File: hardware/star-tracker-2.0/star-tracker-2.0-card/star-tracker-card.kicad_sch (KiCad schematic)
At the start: 8 parts, among them J1 SM14B-SHLS-TF, J101 3-1734592-64-1734592-0, J4 TFM-120-01-L-D-RA, J7 GRPB041VWVN-RC

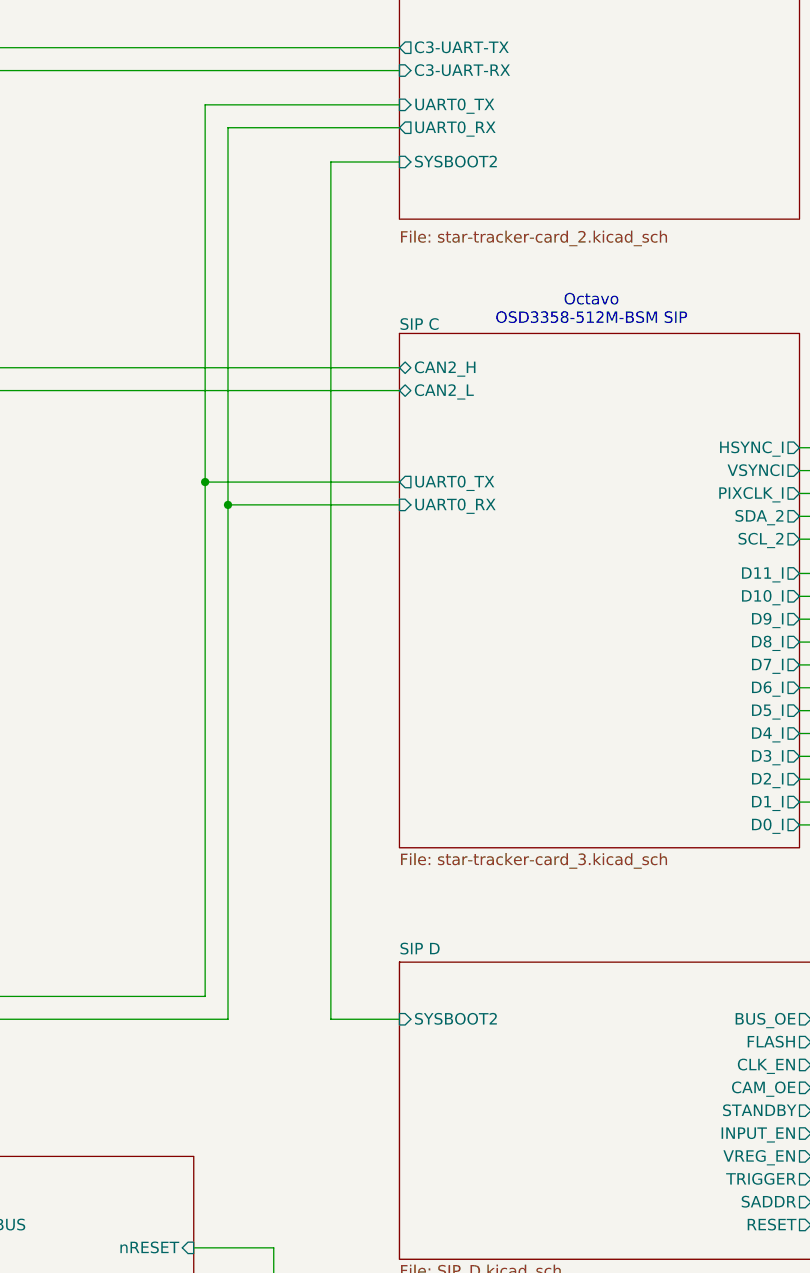
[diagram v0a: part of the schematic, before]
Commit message: Added IMU
added IMU, and i2c pull up resistors to schematic.
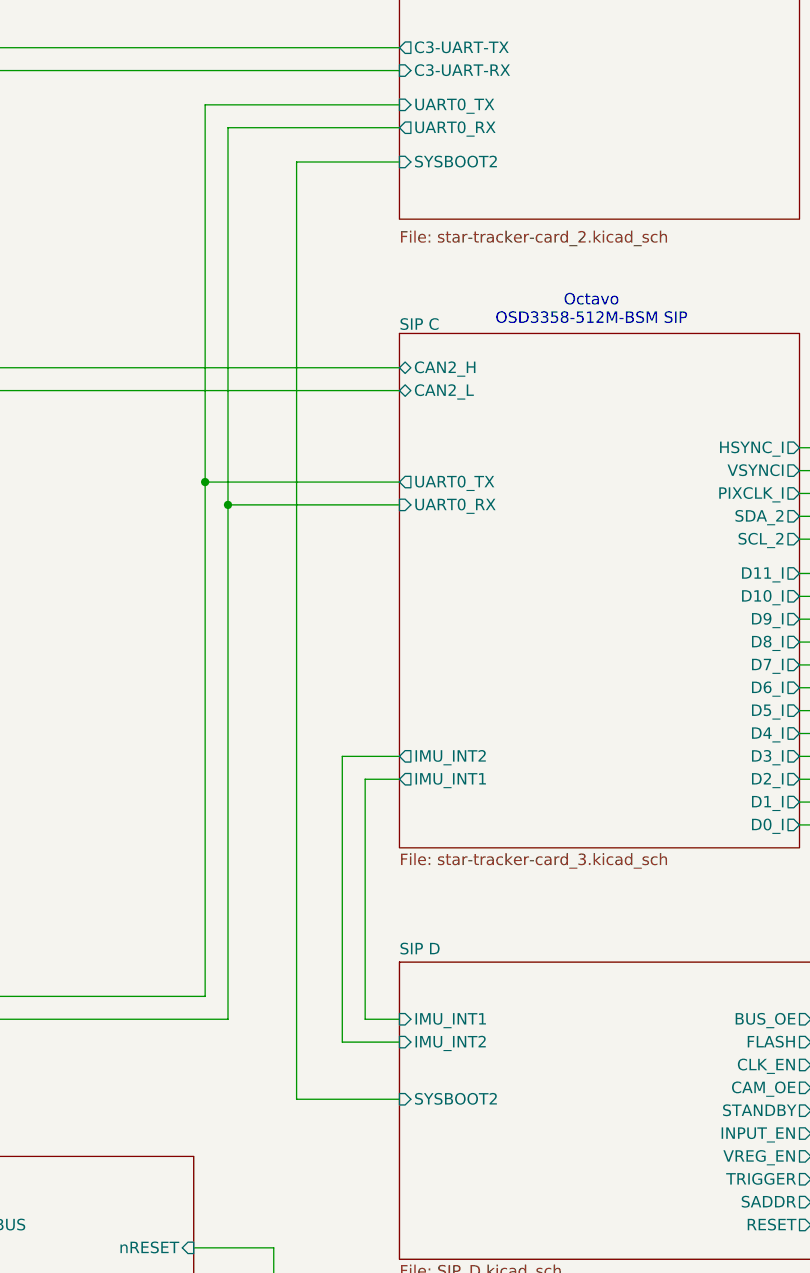
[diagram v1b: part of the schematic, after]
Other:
- sheet SIP C ports: added IMU_INT1, IMU_INT2; removed none
- sheet SIP D ports: added IMU_INT1, IMU_INT2; removed none
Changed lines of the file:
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@@
 	(wire
 		(pts
+			(xy 184.15 179.07) (xy 190.5 179.07)
+		)
+		(stroke
+			(width 0)
+			(type default)
+		)
+	)
+	(wire
+		(pts
 			(xy 386.08 106.68) (xy 386.08 104.14)
 		)
@@
 	(wire
 		(pts
+			(xy 184.15 147.32) (xy 184.15 179.07)
+		)
+		(stroke
+			(width 0)
+			(type default)
+		)
+	)
+	(wire
+		(pts
 			(xy 171.45 119.38) (xy 190.5 119.38)
 		)
@@
 	(wire
 		(pts
+			(xy 190.5 149.86) (xy 186.69 149.86)
+		)
+		(stroke
+			(width 0)
+			(type default)
+		)
+	)
+	(wire
+		(pts
 			(xy 308.61 137.16) (xy 391.16 137.16)
 		)
@@
 	(wire
 		(pts
+			(xy 186.69 149.86) (xy 186.69 176.53)
+		)
+		(stroke
+			(width 0)
+			(type default)
+		)
+	)
+	(wire
+		(pts
 			(xy 46.99 86.36) (xy 49.53 86.36)
 		)
@@
 	(wire
 		(pts
+			(xy 190.5 147.32) (xy 184.15 147.32)
+		)
+		(stroke
+			(width 0)
+			(type default)
+		)
+	)
+	(wire
+		(pts
 			(xy 92.71 199.39) (xy 134.62 199.39)
 		)
@@
 	(wire
 		(pts
+			(xy 186.69 176.53) (xy 190.5 176.53)
+		)
+		(stroke
+			(width 0)
+			(type default)
+		)
+	)
+	(wire
+		(pts
 			(xy 236.22 194.31) (xy 265.43 194.31)
 		)
@@
 	(wire
 		(pts
-			(xy 182.88 81.28) (xy 190.5 81.28)
+			(xy 179.07 81.28) (xy 190.5 81.28)
 		)
 		(stroke
@@
 	(wire
 		(pts
-			(xy 182.88 176.53) (xy 182.88 81.28)
+			(xy 179.07 185.42) (xy 179.07 81.28)
 		)
 		(stroke
@@
 	(wire
 		(pts
-			(xy 190.5 176.53) (xy 182.88 176.53)
+			(xy 190.5 185.42) (xy 179.07 185.42)
 		)
 		(stroke
@@
 		)
 		(pin "SYSBOOT2" input
+			(at 190.5 185.42 180)
+			(effects
+				(font
+					(size 1.27 1.27)
+				)
+				(justify left)
+			)
+		)
+		(pin "IMU_INT1" input
 			(at 190.5 176.53 180)
 			(effects
@@
 			)
 		)
+		(pin "IMU_INT2" input
+			(at 190.5 179.07 180)
+			(effects
+				(font
+					(size 1.27 1.27)
+				)
+				(justify left)
+			)
+		)
 		(instances
 			(project "star-tracker-card"
@@
 			)
 		)
+		(pin "IMU_INT1" output
+			(at 190.5 149.86 180)
+			(effects
+				(font
+					(size 1.27 1.27)
+				)
+				(justify left)
+			)
+		)
+		(pin "IMU_INT2" output
+			(at 190.5 147.32 180)
+			(effects
+				(font
+					(size 1.27 1.27)
+				)
+				(justify left)
+			)
+		)

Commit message: Routine Push
Updated schematic and layout. about 60% done with routing.
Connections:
- net 3.3V: now also J101.4, J101.5, J101.6; no longer J101.31, J101.32, J101.33
- net CLK_EN_E: now also J101.26; no longer J101.23
- net D0_E: now also J101.25; no longer J101.12
- net D10_E: now also J101.12; no longer J101.16
- net D11_E: now also J101.11; no longer J101.17
- net D1_E: now also J101.24; no longer J101.11
- net D2_E: now also J101.23; no longer J101.10
- net D3_E: now also J101.22; no longer J101.9
- net D4_E: now also J101.21; no longer J101.8
- net D5_E: now also J101.20; no longer J101.7
- net D6_E: now also J101.16; no longer J101.6
- net D7_E: now also J101.15; no longer J101.13
- net D9_E: now also J101.13; no longer J101.15
- net FLASH_E: now also J101.31; no longer J101.28
- net GND: now also J101.17, J101.3; no longer J101.20, J101.34
- net HSYNC_E: now also J101.34; no longer J101.4
- net I2C2_SCL: now also J101.9; no longer J101.21
- net I2C2_SDA: now also J101.10; no longer J101.22
- net PIXCLK_E: now also J101.27; no longer J101.5
- net SADDR_E: now also J101.8; no longer J101.27
- net STANDBY_E: now also J101.29; no longer J101.25
- net TRIGGER_E: now also J101.32; no longer J101.29
- net VREG_EN_E: now also J101.7; no longer J101.30
- net VSYNC_E: now also J101.33; no longer J101.3
- net ~{OE_E}: now also J101.30; no longer J101.26
- net ~{RESET_E}: now also J101.28; no longer J101.24
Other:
- moved on the sheet: C42, C43

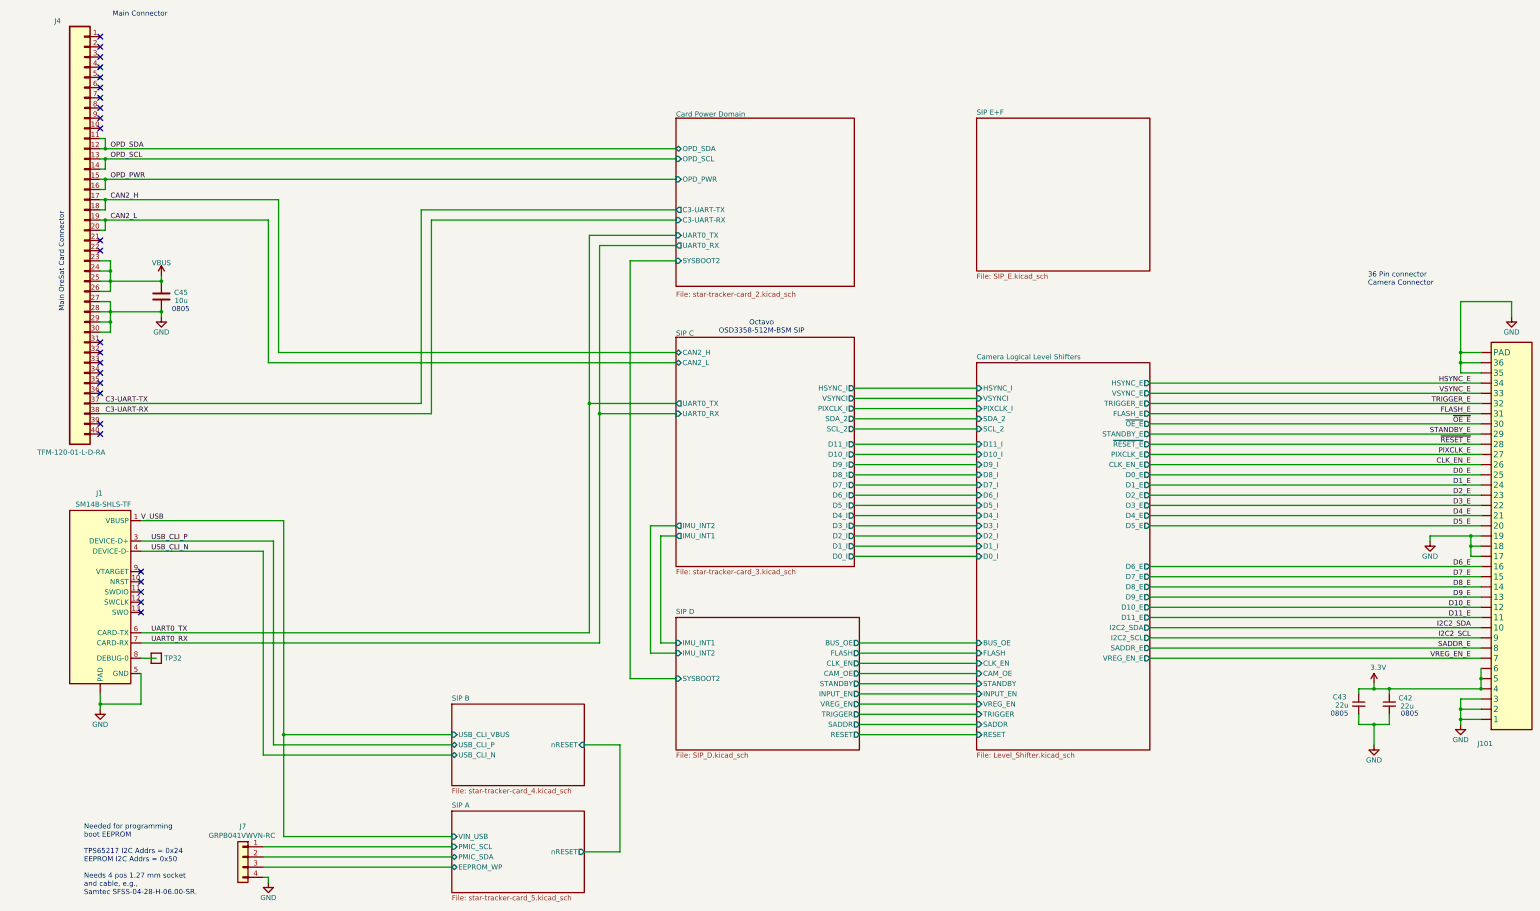
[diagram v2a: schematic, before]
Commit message: Star tracker board update
Added 3d models to footprints, reannotated component designators
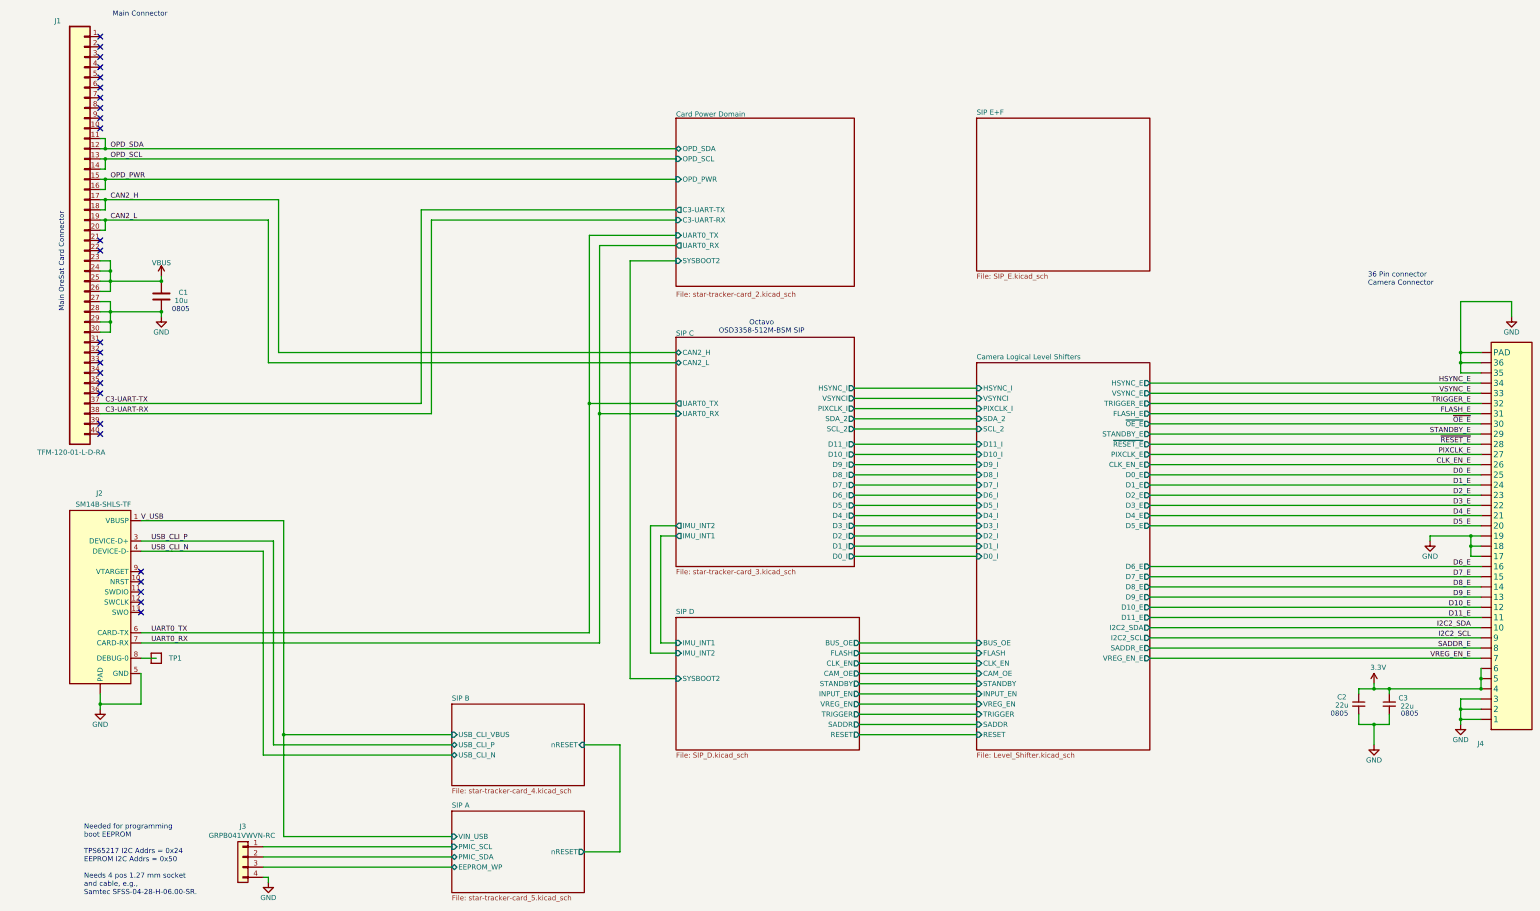
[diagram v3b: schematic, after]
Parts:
- renumbered C45 to C1, C43 to C2, C42 to C3, J4 to J1, J1 to J2, J7 to J3, J101 to J4, TP32 to TP1
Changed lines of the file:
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@@
 	(title_block
 		(title "OreSat Star Tracker")
-		(date "2026-04-22")
-		(rev "1.3")
+		(date "2026-06-05")
+		(rev "2.0")
 		(company "Portland State Aerospace Society")
 	)
@@
 		(in_pos_files yes)
 		(dnp no)
-		(property "Reference" "C42"
+		(property "Reference" "C3"
 			(at 370.586 191.008 0)
 			(show_name no)
@@
 			(project "star-tracker-card"
 				(path "/324e9eb5-7420-4b7e-862c-cc20bb28618a"
-					(reference "C42")
+					(reference "C3")
 					(unit 1)
 				)
@@
 		(in_pos_files yes)
 		(dnp no)
-		(property "Reference" "J1"
+		(property "Reference" "J2"
 			(at 45.974 139.954 0)
 			(show_name no)
@@
 			(project "star-tracker-card"
 				(path "/324e9eb5-7420-4b7e-862c-cc20bb28618a"
-					(reference "J1")
+					(reference "J2")
 					(unit 1)
 				)
@@
 		(in_pos_files yes)
 		(dnp no)
-		(property "Reference" "C45"
+		(property "Reference" "C1"
 			(at 68.834 89.916 0)
 			(show_name no)
@@
 			(project "star-tracker-card"
 				(path "/324e9eb5-7420-4b7e-862c-cc20bb28618a"
-					(reference "C45")
+					(reference "C1")
 					(unit 1)
 				)
@@
 		(in_pos_files yes)
 		(dnp no)
-		(property "Reference" "C43"
+		(property "Reference" "C2"
 			(at 357.632 190.754 0)
 			(show_name no)
@@
 			(project "star-tracker-card"
 				(path "/324e9eb5-7420-4b7e-862c-cc20bb28618a"
-					(reference "C43")
+					(reference "C2")
 					(unit 1)
 				)
@@
 		(in_pos_files yes)
 		(dnp no)
-		(property "Reference" "TP32"
+		(property "Reference" "TP1"
 			(at 67.31 180.34 0)
 			(show_name no)
@@
 			(project "star-tracker-card"
 				(path "/324e9eb5-7420-4b7e-862c-cc20bb28618a"
-					(reference "TP32")
+					(reference "TP1")
 					(unit 1)
 				)
@@
 		(in_pos_files yes)
 		(dnp no)
-		(property "Reference" "#PWR1"
+		(property "Reference" "#PWR02"
 			(at 62.23 101.6 0)
 			(hide yes)
@@
 			(project "star-tracker-card"
 				(path "/324e9eb5-7420-4b7e-862c-cc20bb28618a"
-					(reference "#PWR1")
+					(reference "#PWR02")
 					(unit 1)
 				)
@@
 		(in_pos_files yes)
 		(dnp no)
-		(property "Reference" "#3V-13"
+		(property "Reference" "#3V-01"
 			(at 364.49 184.15 0)
 			(hide yes)
@@
 			(project "star-tracker-card"
 				(path "/324e9eb5-7420-4b7e-862c-cc20bb28618a"
-					(reference "#3V-13")
+					(reference "#3V-01")
 					(unit 1)
 				)
@@
 		(in_pos_files yes)
 		(dnp no)
-		(property "Reference" "#PWR45"
+		(property "Reference" "#PWR06"
 			(at 386.08 203.2 0)
 			(hide yes)
@@
 			(project "star-tracker-card"
 				(path "/324e9eb5-7420-4b7e-862c-cc20bb28618a"
-					(reference "#PWR45")
+					(reference "#PWR06")
 					(unit 1)
 				)
@@
 		(in_pos_files yes)
 		(dnp no)
-		(property "Reference" "#PWR4"
+		(property "Reference" "#PWR04"
 			(at 364.49 208.28 0)
 			(hide yes)
@@
 			(project "star-tracker-card"
 				(path "/324e9eb5-7420-4b7e-862c-cc20bb28618a"
-					(reference "#PWR4")
+					(reference "#PWR04")
 					(unit 1)
 				)
@@
 		(in_pos_files yes)
 		(dnp no)
-		(property "Reference" "#PWR39"
+		(property "Reference" "#PWR07"
 			(at 398.78 101.6 0)
 			(hide yes)
@@
 			(project "star-tracker-card"
 				(path "/324e9eb5-7420-4b7e-862c-cc20bb28618a"
-					(reference "#PWR39")
+					(reference "#PWR07")
 					(unit 1)
 				)
@@
 		(in_pos_files yes)
 		(dnp no)
-		(property "Reference" "J7"
+		(property "Reference" "J3"
 			(at 82.55 222.25 0)
 			(show_name no)
@@
 			(project "star-tracker-card"
 				(path "/324e9eb5-7420-4b7e-862c-cc20bb28618a"
-					(reference "J7")
+					(reference "J3")
 					(unit 1)
 				)
@@
 		(in_pos_files yes)
 		(dnp no)
-		(property "Reference" "#PWR043"
+		(property "Reference" "#PWR05"
 			(at 378.46 157.48 0)
 			(hide yes)
@@
 			(project "star-tracker-card"
 				(path "/324e9eb5-7420-4b7e-862c-cc20bb28618a"
-					(reference "#PWR043")
+					(reference "#PWR05")
 					(unit 1)
 				)
@@
 		(in_pos_files yes)
 		(dnp no)
-		(property "Reference" "J101"
+		(property "Reference" "J4"
 			(at 390.2456 200.8886 0)
 			(show_name no)
@@
 			(project "star-tracker-card"
 				(path "/324e9eb5-7420-4b7e-862c-cc20bb28618a"
-					(reference "J101")
+					(reference "J4")
 					(unit 1)
 				)
@@
 		(in_pos_files yes)
 		(dnp no)
-		(property "Reference" "#PWR76"
+		(property "Reference" "#PWR01"
 			(at 46.99 199.39 0)
 			(hide yes)
@@
 			(project "star-tracker-card"
 				(path "/324e9eb5-7420-4b7e-862c-cc20bb28618a"
-					(reference "#PWR76")
+					(reference "#PWR01")
 					(unit 1)
 				)
@@
 		(in_pos_files yes)
 		(dnp no)
-		(property "Reference" "#PWR54"
+		(property "Reference" "#PWR03"
 			(at 88.9 242.57 0)
 			(hide yes)
@@
 			(project "star-tracker-card"
 				(path "/324e9eb5-7420-4b7e-862c-cc20bb28618a"
-					(reference "#PWR54")
+					(reference "#PWR03")
 					(unit 1)
 				)
@@
 		(in_pos_files yes)
 		(dnp no)
-		(property "Reference" "J4"
+		(property "Reference" "J1"
 			(at 35.56 22.225 0)
 			(show_name no)
@@
 			(project "star-tracker-card"
 				(path "/324e9eb5-7420-4b7e-862c-cc20bb28618a"
-					(reference "J4")
+					(reference "J1")
 					(unit 1)
 				)

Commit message: Bom update
Updated BOM to correct connector MPN and other misc components
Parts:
- J4: value 3-1734592-64-1734592-0 -> 3-2492104-6; DPN A100290CT-ND -> 17-3-2492104-6CT-ND; MPN 3-1734592-0 -> 3-2492104-6
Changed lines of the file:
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@@
 			)
 		)
-		(property "Value" "3-1734592-64-1734592-0"
+		(property "Value" "3-2492104-6"
 			(at 398.78 147.32 0)
 			(hide yes)
@@
 			)
 		)
-		(property "Datasheet" "https://www.te.com/usa-en/product-3-1734592-0.datasheet.pdf"
+		(property "Datasheet" "https://www.te.com/commerce/DocumentDelivery/DDEController?Action=srchrtrv&DocNm=2492104&DocType=Customer%20Drawing&DocLang=English&DocFormat=pdf&PartCntxt=3-2492104-6"
 			(at 398.78 147.32 0)
 			(hide yes)
@@
 			)
 		)
-		(property "Description" "30 Position FPC Connector Contacts, Bottom 0.020\" (0.50mm) Surface Mount, Right Angle"
+		(property "Description" "36 Position FPC Connector Contacts, Bottom 0.020\" (0.50mm) Surface Mount, Right Angle"
 			(at 398.78 147.32 0)
 			(hide yes)
@@
 			)
 		)
-		(property "DPN" "A100290CT-ND"
+		(property "DPN" "17-3-2492104-6CT-ND"
 			(at 398.78 147.32 0)
 			(hide yes)
@@
 			)
 		)
-		(property "MPN" "3-1734592-0"
+		(property "MPN" "3-2492104-6"
 			(at 398.78 147.32 0)
 			(hide yes)
@@
 		)
 		(fill
-			(color 0 0 0 0)
+			(color 255 229 191 1)
 		)
 		(property "Sheetname" "SIP B"
@@
 		)
 		(fill
-			(color 0 0 0 0)
+			(color 255 229 191 1)
 		)
 		(property "Sheetname" "SIP A"
@@
 		)
 		(fill
-			(color 0 0 0 0)
+			(color 255 229 191 1)
 		)
 		(property "Sheetname" "Card Power Domain"
@@
 		)
 		(fill
-			(color 0 0 0 0)
+			(color 255 229 191 1)
 		)
 		(property "Sheetname" "Camera Logical Level Shifters"
@@
 		)
 		(fill
-			(color 0 0 0 0)
+			(color 255 229 191 1)
 		)
 		(property "Sheetname" "SIP D"
@@
 		)
 		(fill
-			(color 0 0 0 0)
+			(color 255 229 191 1)
 		)
 		(property "Sheetname" "SIP C"
@@
 		)
 		(fill
-			(color 0 0 0 0)
+			(color 255 229 191 1)
 		)
 		(property "Sheetname" "SIP E+F"

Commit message: Component linking
Linked components to 3d models
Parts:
- C1: DPN 490-GRT21BC71E106KE13KCT-ND -> 1276-CL21B106KAYQNNETR-ND; MFR Murata Electronics -> Samsung Electro-Mechanics; MPN GRT21BC71E106KE13K -> CL21B106KAYQNNE
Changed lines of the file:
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@@
 			)
 		)
-		(property "Datasheet" "https://search.murata.co.jp/Ceramy/image/img/A01X/G101/ENG/GRT21BC71E106KE13-01.pdf"
+		(property "Datasheet" "https://mm.digikey.com/Volume0/opasdata/d220001/medias/docus/7851/1276_CL21B1.pdf"
 			(at 62.23 90.17 0)
 			(hide yes)
@@
 			)
 		)
-		(property "Description" "10 µF ±10% 25V Ceramic Capacitor X7S 0805 (2012 Metric)"
+		(property "Description" "10 µF ±10% 25V Ceramic Capacitor X7R 0805 (2012 Metric)"
 			(at 62.23 90.17 0)
 			(hide yes)
@@
 			)
 		)
-		(property "DPN" "490-GRT21BC71E106KE13KCT-ND"
+		(property "DPN" "1276-CL21B106KAYQNNETR-ND"
 			(at 62.23 90.17 0)
 			(hide yes)
@@
 			)
 		)
-		(property "MFR" "Murata Electronics"
+		(property "MFR" "Samsung Electro-Mechanics"
 			(at 62.23 90.17 0)
 			(hide yes)
@@
 			)
 		)
-		(property "MPN" "GRT21BC71E106KE13K"
+		(property "MPN" "CL21B106KAYQNNE"
 			(at 62.23 90.17 0)
 			(hide yes)
